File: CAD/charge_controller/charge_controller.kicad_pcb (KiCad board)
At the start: 2 copper layers, 100 x 50 mm, 60 parts, among them J1 SENSE, J2 PSU, J3 ENABLE, J4 BATT, J5 FB, Q1 Q_NMOS_SDG, Q2 Q_PMOS_GDS, Q3 MMBT3904, Q4 Q_PMOS_GDS, U1 LMV324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

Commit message: progress on charge and output layout
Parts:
- removed JP2, JP5: V_Sel, Connector_PinHeader_2.54mm:PinHeader_1x03_P2.54mm_Vertical
- removed JP6, JP7: Jumper_NC_Small, Jumper:SolderJumper-2_P1.3mm_Bridged_Pad1.0x1.5mm
- added C8: 0.1uF, Capacitor_SMD:C_0603_1608Metric, F.Cu at (174.8, 141.6)
- added C9: NC, Capacitor_SMD:C_0603_1608Metric, F.Cu at (180.0, 141.6)
- added D5: 12V, Diode_SMD:D_SOD-523, F.Cu at (139.0, 116.5)
- added D6: 12V, Diode_SMD:D_SOD-523, F.Cu at (158.5, 118.0)
- added D7: D_Schottky, Diode_SMD:D_SOD-523, F.Cu at (184.1, 137.6)
- added J6: Conn_02x03_Odd_Even, Connector_PinHeader_2.54mm:PinHeader_2x03_P2.54mm_Vertical_SMD, F.Cu at (146.0, 136.0)
- added J7: CHARGE_VI, Connector_PinSocket_2.54mm:PinSocket_1x03_P2.54mm_Vertical, F.Cu at (181.5, 147.0)
- added L1: L_Small, Inductor_SMD:L_0603_1608Metric, F.Cu at (174.8, 145.6)
- added Q5: Q_NMOS_SDG, Package_TO_SOT_SMD:SOT-23, F.Cu at (162.0, 118.0)
- added R24: R_Small, Resistor_SMD:R_0603_1608Metric, F.Cu at (159.0, 133.5)
- added R25: 100, Resistor_SMD:R_0603_1608Metric, F.Cu at (135.5, 118.0)
- added R26: 1K, Resistor_SMD:R_0603_1608Metric, F.Cu at (137.0, 136.0)
- added R27: 1K, Resistor_SMD:R_0603_1608Metric, F.Cu at (153.0, 117.0)
- added R28: 10K, Resistor_SMD:R_0603_1608Metric, F.Cu at (156.0, 118.0)
- added R29: 56K, Resistor_SMD:R_0603_1608Metric, F.Cu at (120.5, 143.0)
- added R30: NC, Resistor_SMD:R_0603_1608Metric, F.Cu at (177.8, 127.6)
- added R31: 56K, Resistor_SMD:R_0603_1608Metric, F.Cu at (177.5, 141.5)
- added R32: 0.1R, Resistor_SMD:R_1206_3216Metric, F.Cu at (179.0, 121.0)
- added R33: 0.1R, Resistor_SMD:R_1206_3216Metric, F.Cu at (182.0, 121.0)
- added R34: 56K, Resistor_SMD:R_0603_1608Metric, F.Cu at (180.0, 137.0)
- added R35: 0.1R, Resistor_SMD:R_1206_3216Metric, F.Cu at (185.0, 121.0)
- added R36: 0.1R, Resistor_SMD:R_1206_3216Metric, F.Cu at (188.0, 121.0)
- added R37: 1K, Resistor_SMD:R_0603_1608Metric, F.Cu at (189.0, 129.0)
- added R38: 10K, Resistor_SMD:R_0603_1608Metric, F.Cu at (189.0, 127.0)
- C4: value C_Small -> NC
- J1: value SENSE -> MCU; footprint Connector_Phoenix_MC:PhoenixContact_MCV_1,5_2-G-5.08_1x02_P5.08mm_Vertical -> Connector_PinSocket_2.54mm:PinSocket_1x04_P2.54mm_Vertical
- J3: value ENABLE -> Conn_02x03_Odd_Even; footprint Connector_Phoenix_MC:PhoenixContact_MCV_1,5_2-G-5.08_1x02_P5.08mm_Vertical -> Connector_PinHeader_2.54mm:PinHeader_2x03_P2.54mm_Vertical_SMD
- J5: footprint Connector_Phoenix_MC:PhoenixContact_MCV_1,5_2-G-5.08_1x02_P5.08mm_Vertical -> Connector_Phoenix_MC:PhoenixContact_MCV_1,5_3-G-5.08_1x03_P5.08mm_Vertical
- R10: value 620K -> 56K
- R12: value 1M -> 100K
- R13: value 430K -> 10K
- R17: value 200K -> 20K
- R21: value R_Small -> NC
- moved F1 59.0 mm to (126.0, 109.0)
- moved R7 44.6 mm to (139.0, 119.0)
- moved R3 42.9 mm to (127.5, 119.0)
- moved Q3 42.7 mm to (132.0, 118.0)
- moved Q2 42.4 mm to (136.0, 109.0)
- moved R6 42.4 mm to (127.5, 116.5)
- moved J3 42.2 mm to (146.0, 125.0), turned to 180 degrees
- moved Q4 42.2 mm to (146.0, 109.0)
- moved R1 36.5 mm to (182.5, 132.6), turned to 90 degrees
- moved R47 34.0 mm to (156.0, 122.0), turned to 270 degrees
- moved R2 33.4 mm to (180.0, 132.6), turned to 270 degrees
- moved D1 32.8 mm to (155.0, 126.0), turned to 270 degrees
- moved JP3 32.6 mm to (159.0, 126.0), turned to 270 degrees
- moved R18 32.6 mm to (117.5, 143.0)
- moved JP4 30.0 mm to (171.8, 145.6), turned to 90 degrees
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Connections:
- C2 pad 2: +12V -> Net-(C2-Pad2)
- C21 pad 2: /OP_12V -> +12V
- C5 pad 1: GND -> Net-(C5-Pad1)
- C5 pad 2: Net-(C5-Pad2) -> +BATT
- C6 pad 1: GND -> Net-(C5-Pad1)
- C6 pad 2: Net-(C5-Pad2) -> +BATT
- C7 pad 1: GND -> Net-(C7-Pad1)
- D2 pad 1: Net-(D2-Pad1) -> /BOOST_FB
- D3 pad 1: Net-(D3-Pad1) -> /BOOST_FB
- D4 pad 2: Net-(D4-Pad2) -> /chrg_en
- F1 pad 1: Net-(C5-Pad2) -> +VDC
- F1 pad 2: +BATT -> Net-(F1-Pad2)
- J1 pad 1: Net-(J1-Pad1) -> /chrg_en
- J1 pad 2: GND -> /trickle_dis
- J2 pad 2: +VDC -> Net-(F1-Pad2)
- J3 pad 1: GND -> Net-(J3-Pad1)
- J3 pad 2: Net-(D4-Pad2) -> Net-(D1-Pad2)
- J4 pad 1: Net-(C5-Pad2) -> +BATT
- J4 pad 2: GND -> Net-(C5-Pad1)
- J5 pad 1: boost_fb -> /chrg_in_v
- J5 pad 2: GND -> /BOOST_FB
- JP1 pad 1: +VDC -> Net-(JP1-Pad1)
- JP4 pad 2: /batt_ref -> /batt_v
- L10 pad 1: /OP_12V -> +12V
- L10 pad 2: +12V -> Net-(C2-Pad2)
- Q2 pad 1: Net-(Q2-Pad1) -> Net-(D5-Pad2)
- Q2 pad 3: Net-(Q2-Pad3) -> Net-(D5-Pad1)
- Q3 pad 3: Net-(Q2-Pad1) -> Net-(Q3-Pad3)
- Q4 pad 1: Net-(Q2-Pad1) -> Net-(D5-Pad2)
- Q4 pad 2: Net-(Q2-Pad3) -> +BATT
- Q4 pad 3: +BATT -> Net-(D5-Pad1)
- R10 pad 1: Net-(R10-Pad1) -> Net-(J3-Pad3)
- R11 pad 1: Net-(JP2-Pad3) -> Net-(J3-Pad1)
- R13 pad 1: Net-(R10-Pad1) -> Net-(JP1-Pad1)
- R13 pad 2: Net-(Q1-Pad3) -> +VDC
- R17 pad 2: GND -> Net-(C7-Pad1)
- R18 pad 1: /batt_ref -> Net-(Q1-Pad3)
- R18 pad 2: Net-(R18-Pad2) -> /trickle_dis
- R2 pad 1: /batt_current -> /chrg_i
- R21 pad 1: /batt_current -> Net-(R21-Pad1)
- R23 pad 1: /batt_ref -> /batt_v
- R4 pad 2: Net-(JP2-Pad1) -> Net-(J3-Pad5)
- R5 pad 1: Net-(JP2-Pad1) -> Net-(J3-Pad5)
- R7 pad 1: Net-(Q2-Pad3) -> Net-(D5-Pad1)
- R7 pad 2: Net-(Q2-Pad1) -> Net-(D5-Pad2)
- R8 pad 2: Net-(JP2-Pad3) -> Net-(J3-Pad1)
- R9 pad 1: /V_ref -> +12V
- R9 pad 2: Net-(R10-Pad1) -> Net-(J3-Pad3)
- U1 pad 1: /batt_current -> /chrg_i
- U1 pad 12: Net-(R10-Pad1) -> Net-(C8-Pad1)
- U1 pad 13: Net-(R18-Pad2) -> Net-(C9-Pad2)
- U1 pad 14: Net-(Q1-Pad3) -> Net-(D7-Pad2)
- U1 pad 3: Net-(J1-Pad1) -> Net-(C5-Pad1)
- U1 pad 4: /OP_12V -> +12V
- U1 pad 5: /batt_current -> Net-(R21-Pad1)
- U2 pad 3: +12V -> Net-(C2-Pad2)

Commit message: finishes layout for mcu controller
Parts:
- moved JP4 28.1 mm to (171.8, 117.5), turned to 0 degrees
- moved R20 9.12 mm to (156.5, 142.5), turned to 180 degrees
- moved R12 8.22 mm to (165.5, 114.0), turned to 270 degrees
- moved C1 6.10 mm to (121.0, 119.5)
- moved C2 6.10 mm to (121.0, 131.5)
- moved L10 6.10 mm to (127.0, 135.0)
- moved U2 6.10 mm to (124.0, 125.5)
- moved R11 6.00 mm to (137.0, 122.0)
- moved R4 6.00 mm to (133.0, 128.0)
- moved R5 6.00 mm to (137.0, 128.0)
- moved R8 6.00 mm to (133.0, 122.0)
- moved R16 5.50 mm to (137.0, 133.5)
- moved R19 5.50 mm to (137.0, 138.5)
- moved Q1 2.50 mm to (156.5, 137.0)
- moved R14 2.50 mm to (156.5, 140.0), turned to 180 degrees
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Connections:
- net Net-(C2-Pad2) renamed /12V_O
- net Net-(C5-Pad1) renamed /BATT_SENSE
- net Net-(D5-Pad1) renamed /VIN_BATT
- net Net-(F1-Pad2) renamed /VIN
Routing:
- net +12V: track 0.00 -> 83.3 mm
- net GND: track 0.00 -> 76.0 mm, vias 0 -> 39
- net Net-(L1-Pad1): track 0.00 -> 58.1 mm
- net /V_ref: track 0.00 -> 56.5 mm, vias 0 -> 3
- net +VDC: track 0.00 -> 52.6 mm
- net /batt_v: track 0.00 -> 46.7 mm, vias 0 -> 2
- net Net-(Q1-Pad3): track 0.00 -> 46.1 mm
- net Net-(D4-Pad1): track 0.00 -> 46.0 mm, vias 0 -> 2
- net Net-(J6-Pad1): track 0.00 -> 43.1 mm
- net /BOOST_FB: track 0.00 -> 36.4 mm, vias 0 -> 2
- net /chrg_i: track 0.00 -> 33.0 mm, vias 0 -> 2
- net +BATT: track 0.00 -> 25.2 mm
- net /chrg_v: track 0.00 -> 22.8 mm, vias 0 -> 2
- net Net-(D5-Pad2): track 0.00 -> 18.3 mm, vias 0 -> 2
- net /BATT_SENSE: track 0.00 -> 15.1 mm
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- added copper zone on F.Cu, net +BATT
- added copper zone on F.Cu, net +VDC
- added copper zone on F.Cu, net /BATT_SENSE
- added copper zone on F.Cu, net /VIN
- added copper zone on F.Cu, net /VIN_BATT
- added copper zone on B.Cu, net GND
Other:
- net class Default: clearance 0.2 -> 0.25
- net class PWR added: clearance 0.25, trace_width 0.5, via_dia 0.8, via_drill 0.4
- rule trace_clearance: 0.2 -> 0.25

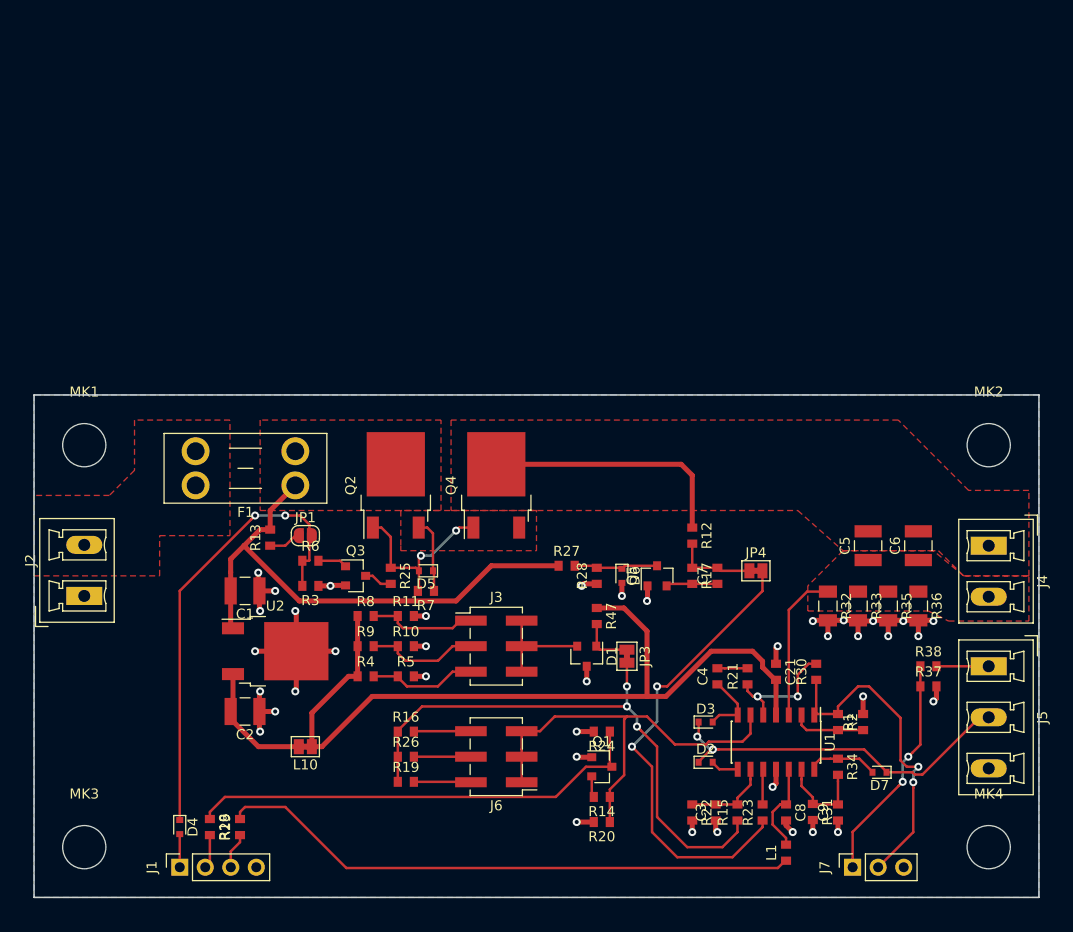
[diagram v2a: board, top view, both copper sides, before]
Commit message: removes pin 17 connection to VIN on mcu controller
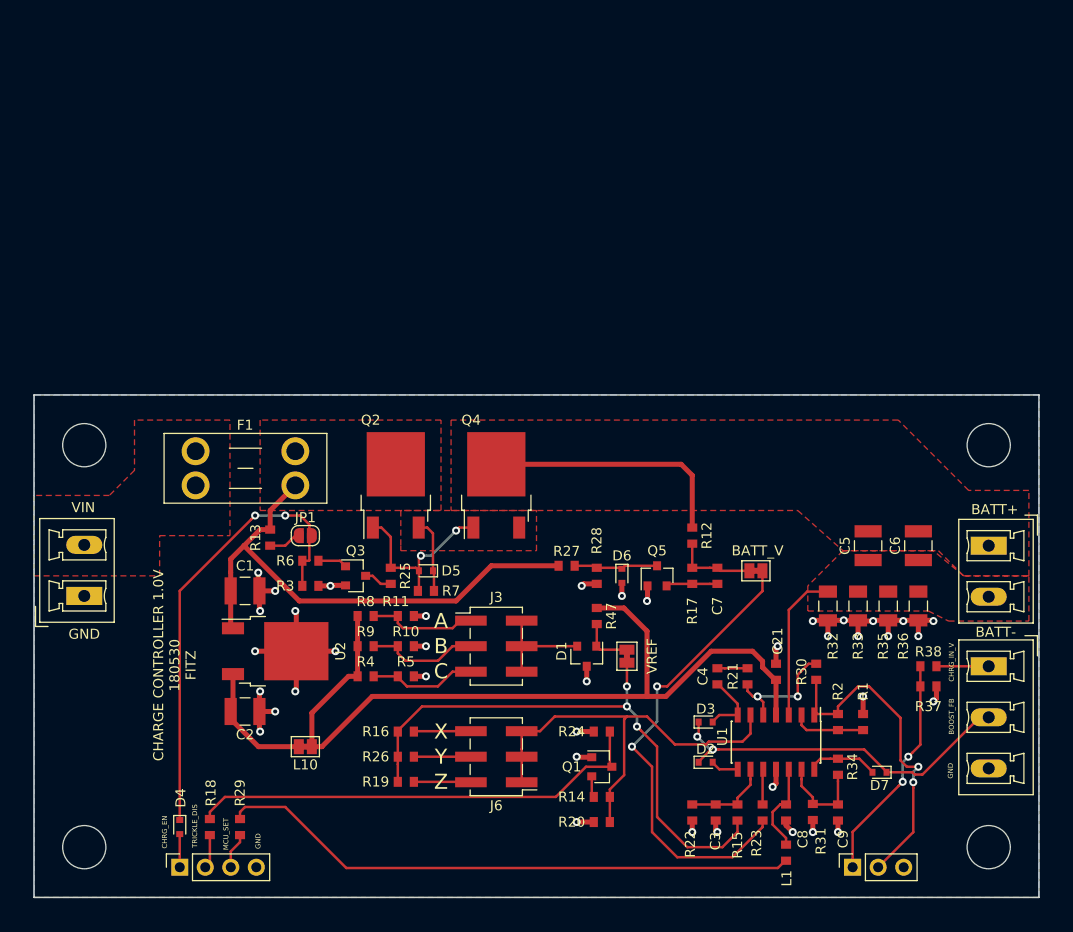
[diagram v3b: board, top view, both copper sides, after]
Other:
- board text added: "A"
- board text added: "B"
- board text added: "BATT+"
- board text added: "BATT-"
- board text added: "BATT_V"
- board text added: "BOOST_FB"
- board text added: "C"
- board text added: "CHARGE CONTROLLER 1.0V 180530 FITZ"
- board text added: "CHRG_EN"
- board text added: "CHRG_IN_V"
- board text added: "GND"
- board text added: "MCU_SET"
- board text added: "TRICKLE_DIS"
- board text added: "VIN"
- board text added: "VREF"
- board text added: "X"
- board text added: "Y"
- board text added: "Z"
